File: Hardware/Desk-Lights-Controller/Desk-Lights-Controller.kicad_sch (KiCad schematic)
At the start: 0 parts

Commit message: Added schematics
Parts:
- added C1: 10u, Capacitor_THT:CP_Radial_D6.3mm_P2.50mm, symbol Device:C_Polarized_US
- added C2, C4: 1u, Capacitor_SMD:C_0805_2012Metric, symbol Device:C
- added C3, C5, C6, C7, C8: 100n, Capacitor_SMD:C_0805_2012Metric, symbol Device:C
- added F1: Fuse, Fuse:Fuseholder_Cylinder-5x20mm_Schurter_0031_8201_Horizontal_Open, symbol Device:Fuse
- added J1, J2, J3: 2604-1102, Wago-2604-1102:26041102, symbol Wago-2604-1102:2604-1102
- added J4: 2604-1103, Wago-2604-1103:26041103, symbol Wago-2604-1103:2604-1102
- added K1, K2: Relay_SPDT, Relay_THT:Relay_SPDT_Finder_40.51, symbol Relay:Relay_SPDT
- added PS1: IRM-20-5, Converter_ACDC:Converter_ACDC_MeanWell_IRM-20-xx_THT, symbol Converter_ACDC:IRM-20-5
- added Q1, Q2: BC817, Package_TO_SOT_SMD:SOT-23, symbol Transistor_BJT:BC817
- added R1, R4: 4.7k, Resistor_SMD:R_0805_2012Metric, symbol Device:R
- added R10, R2, R3, R5, R6, R7, R8, R9: 10k, Resistor_SMD:R_0805_2012Metric, symbol Device:R
- added S1, S2, S3: D2FS-FL-N, D2FS-FL-N:D2FSFLN, symbol D2FS-FL-N:D2FS-FL-N
- added U1: XIAO-SAMD21-SMD, Seeed Studio XIAO Series Library:XIAO-SAMD21-SMD, symbol Seeed_Studio_XIAO_Series:XIAO-SAMD21-SMD
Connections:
- new net: Q1.1 (B), R1.1, R2.2
- new net: K1.A2, Q1.3 (C)
- new net: F1.1, J1.1 (1.1), J1.2 (1.2)
- new net: R8.2, S2.2 (NO)
- new net: R5.2, S3.2 (NO)
- new net: Q2.1 (B), R3.2, R4.1
- new net: K2.A2, Q2.3 (C)
- new net +3.3V: R6.2, R7.2, R9.2, U1.12 (3V3)
- new net +5V: C1.1, C2.1, C3.1, C4.1, C5.1, J4.1 (1.1), J4.2 (1.2), K1.A1, K2.A1, PS1.4 (+Vo), U1.14 (5V)
- new net Button-1: C7.1, R7.1, R8.1, U1.4 (PA11_A3_D3)
- new net Button-2: C6.1, R5.1, R6.1
- new net Button-3: C8.1, R10.1, R9.1, U1.5 (PA8_A4_D4_SDA), U1.6 (PA9_A5_D5_SCL)
- new net Data: J4.3 (2.1), J4.4 (2.2), U1.7 (PB08_A6_D6_TX)
- new net GND: C1.2, C2.2, C3.2, C4.2, C5.2, C6.2, C7.2, C8.2, J4.5 (3.1), J4.6 (3.2), PS1.3 (-Vo), Q1.2 (E), Q2.2 (E), R1.2, R10.2, R4.2, S1.1 (COM), S1.2 (NO), S1.3 (DUMMY), S2.1 (COM), S2.3 (DUMMY), S3.1 (COM), S3.3 (DUMMY), U1.13 (GND), U1.16 (GND), U1.20 (GND)
- new net L-in: F1.2, K1.11, K2.11, PS1.1 (AC/L)
- new net L1-out: J2.1 (1.1), J2.2 (1.2), K1.14
- new net L2-out: J3.1 (1.1), J3.2 (1.2), K2.14
- new net Lamp-1: R3.1, U1.2 (PA4_A1_D1)
- new net Lamp-2: R2.1, U1.3 (PA10_A2_D2)
- new net N: J1.3 (2.1), J1.4 (2.2), J2.3 (2.1), J2.4 (2.2), J3.3 (2.1), J3.4 (2.2), PS1.2 (AC/N)
- no-connect marks 0 -> 11

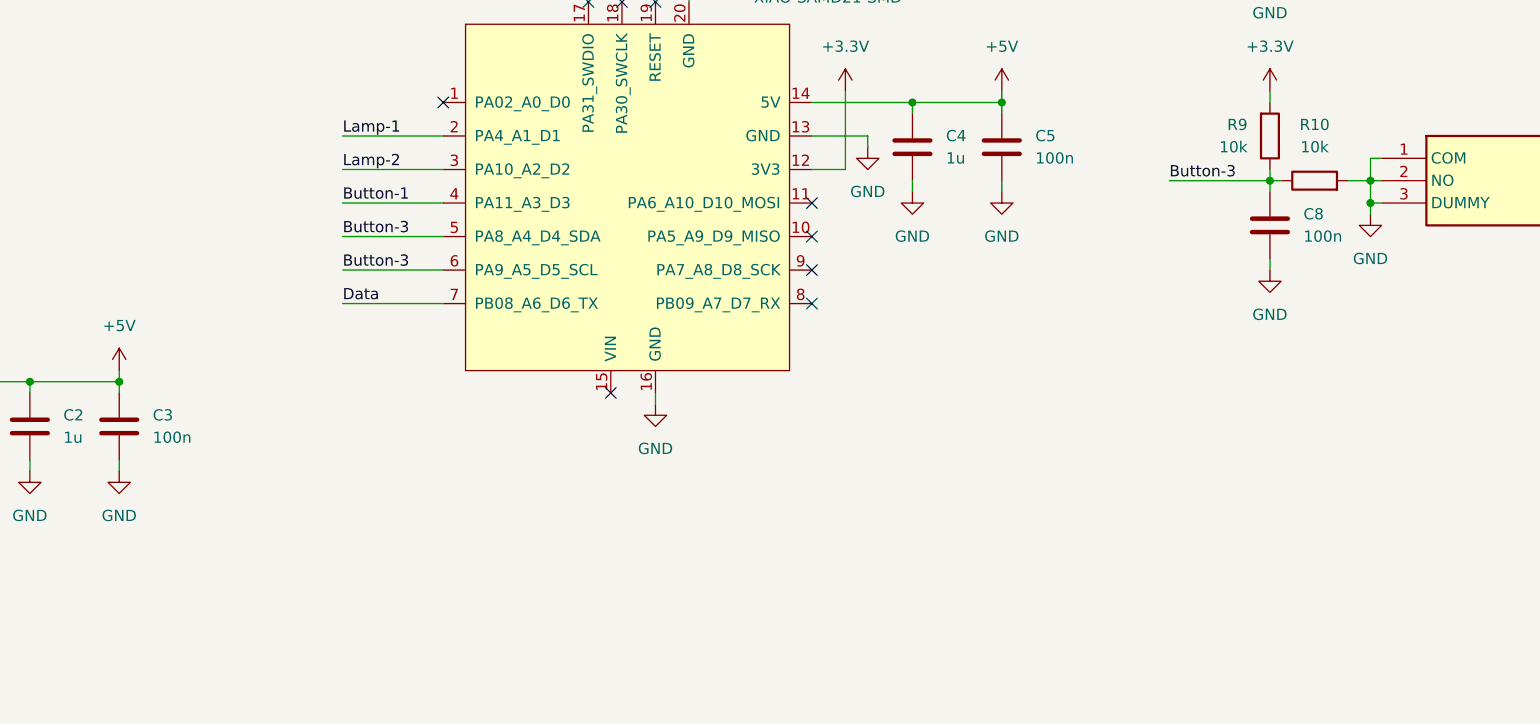
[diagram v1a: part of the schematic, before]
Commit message: Designed PCB, but it might be worth to shrink it a little bit
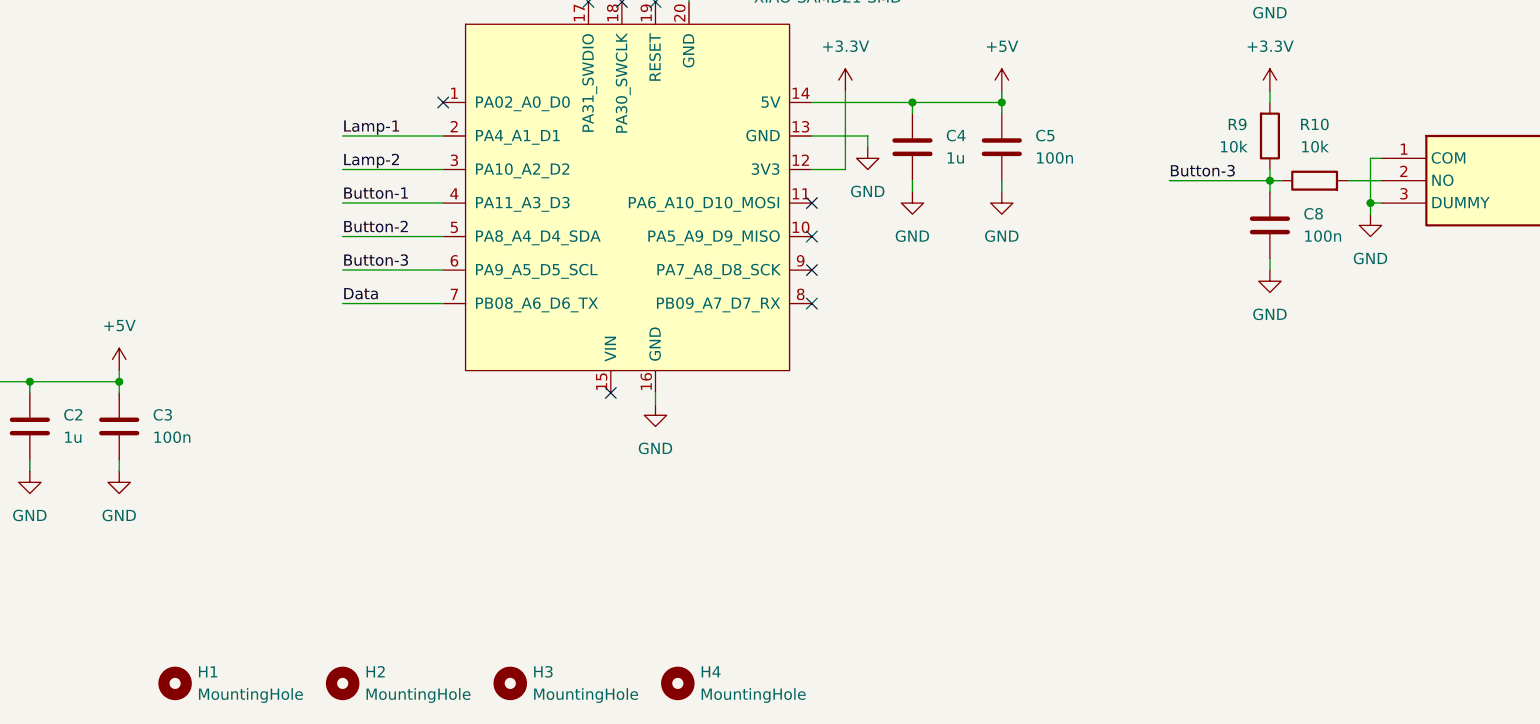
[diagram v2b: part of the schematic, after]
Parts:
- added H1, H2, H3, H4: MountingHole, MountingHole:MountingHole_3.2mm_M3, symbol Mechanical:MountingHole
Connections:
- net Button-2: now also U1.5 (PA8_A4_D4_SDA)
- net Button-3: no longer U1.5 (PA8_A4_D4_SDA)
- net GND: no longer R10.2, S1.2 (NO)
- new net: R10.2, S1.2 (NO)
